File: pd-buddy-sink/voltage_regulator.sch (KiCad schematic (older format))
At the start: 5 parts, among them U1 AP2204R-3.3TRG1

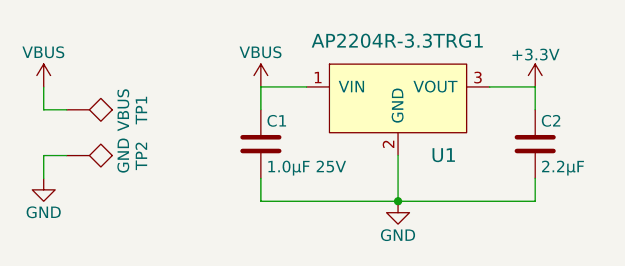
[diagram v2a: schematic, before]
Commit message: Updated schematic with official AP2204R-3.3 symbol
Now that my pull request for the AP2204 regulators has been merged, I
can finally update the PD Buddy Sink schematic to use it.
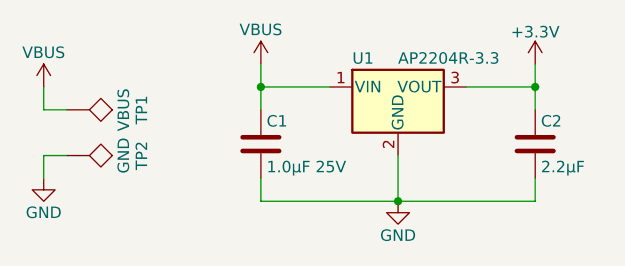
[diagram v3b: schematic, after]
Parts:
- removed U1: AP2204R-3.3TRG1, TO_SOT_Packages_SMD:SOT-89-3, symbol AP2204R-3.3TRG1
- added U1: AP2204R-3.3, TO_SOT_Packages_SMD:SOT-89-3, symbol AP2204R-3.3
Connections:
- net +3V3: now also U1.3 (VOUT)
- net GND: now also U1.2 (GND)
- net VBUS: now also U1.1 (VIN)
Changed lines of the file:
@@
 $EndDescr
 Wire Wire Line
-	5450 3500 5450 3600
+	5450 3400 5450 3600
 Connection ~ 6050 4000
 Wire Wire Line
@@
 	6650 4000 6650 3900
 Wire Wire Line
-	6650 3500 6650 3600
+	6650 3400 6650 3600
 $Comp
 L C C2
@@
 	6050 3800 6050 4000
 Wire Wire Line
-	6450 3500 6650 3500
+	6350 3500 6650 3500
 Wire Wire Line
-	5450 3500 5650 3500
+	5450 3500 5750 3500
 $Comp
 L GND #PWR03
@@
 L +3.3V #PWR04
 U 1 1 588FA3FC
-P 6650 3500
-F 0 "#PWR04" H 6650 3350 50  0001 C CNN
-F 1 "+3.3V" H 6650 3640 50  0000 C CNN
-F 2 "" H 6650 3500 50  0000 C CNN
-F 3 "" H 6650 3500 50  0000 C CNN
-	1    6650 3500
+P 6650 3400
+F 0 "#PWR04" H 6650 3250 50  0001 C CNN
+F 1 "+3.3V" H 6650 3540 50  0000 C CNN
+F 2 "" H 6650 3400 50  0000 C CNN
+F 3 "" H 6650 3400 50  0000 C CNN
+	1    6650 3400
 	1    0    0    -1
 $EndComp
@@
 	4500 3800 4500 3900
 $Comp
-L AP2204R-3.3TRG1 U1
-U 1 1 592B31D5
-P 6050 3500
-F 0 "U1" H 6250 3200 60  0000 C CNN
-F 1 "AP2204R-3.3TRG1" H 6050 3700 60  0000 C CNN
-F 2 "TO_SOT_Packages_SMD:SOT-89-3" H 6150 3100 60  0001 C CNN
-F 3 "http://www.diodes.com/_files/datasheets/AP2204.pdf" H 6250 3200 60  0001 C CNN
-	1    6050 3500
-	1    0    0    -1
-$EndComp
-$Comp
 L VBUS #PWR06
 U 1 1 592B5581
-P 5450 3500
-F 0 "#PWR06" H 5450 3350 50  0001 C CNN
-F 1 "VBUS" H 5450 3650 50  0000 C CNN
-F 2 "" H 5450 3500 50  0001 C CNN
-F 3 "" H 5450 3500 50  0001 C CNN
-	1    5450 3500
+P 5450 3400
+F 0 "#PWR06" H 5450 3250 50  0001 C CNN
+F 1 "VBUS" H 5450 3550 50  0000 C CNN
+F 2 "" H 5450 3400 50  0001 C CNN
+F 3 "" H 5450 3400 50  0001 C CNN
+	1    5450 3400
 	1    0    0    -1
 $EndComp
@@
 	1    0    0    -1
 $EndComp
+$Comp
+L AP2204R-3.3 U1
+U 1 1 5961518D
+P 6050 3500
+F 0 "U1" H 5850 3625 50  0000 L CNN
+F 1 "AP2204R-3.3" H 6050 3625 50  0000 L CNN
+F 2 "TO_SOT_Packages_SMD:SOT-89-3" H 6050 3725 50  0001 C CNN
+F 3 "" H 6050 3500 50  0001 C CNN
+	1    6050 3500
+	1    0    0    -1
+$EndComp
+Connection ~ 5450 3500
+Connection ~ 6650 3500
 $EndSCHEMATC
